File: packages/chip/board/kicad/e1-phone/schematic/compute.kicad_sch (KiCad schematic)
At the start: 0 parts

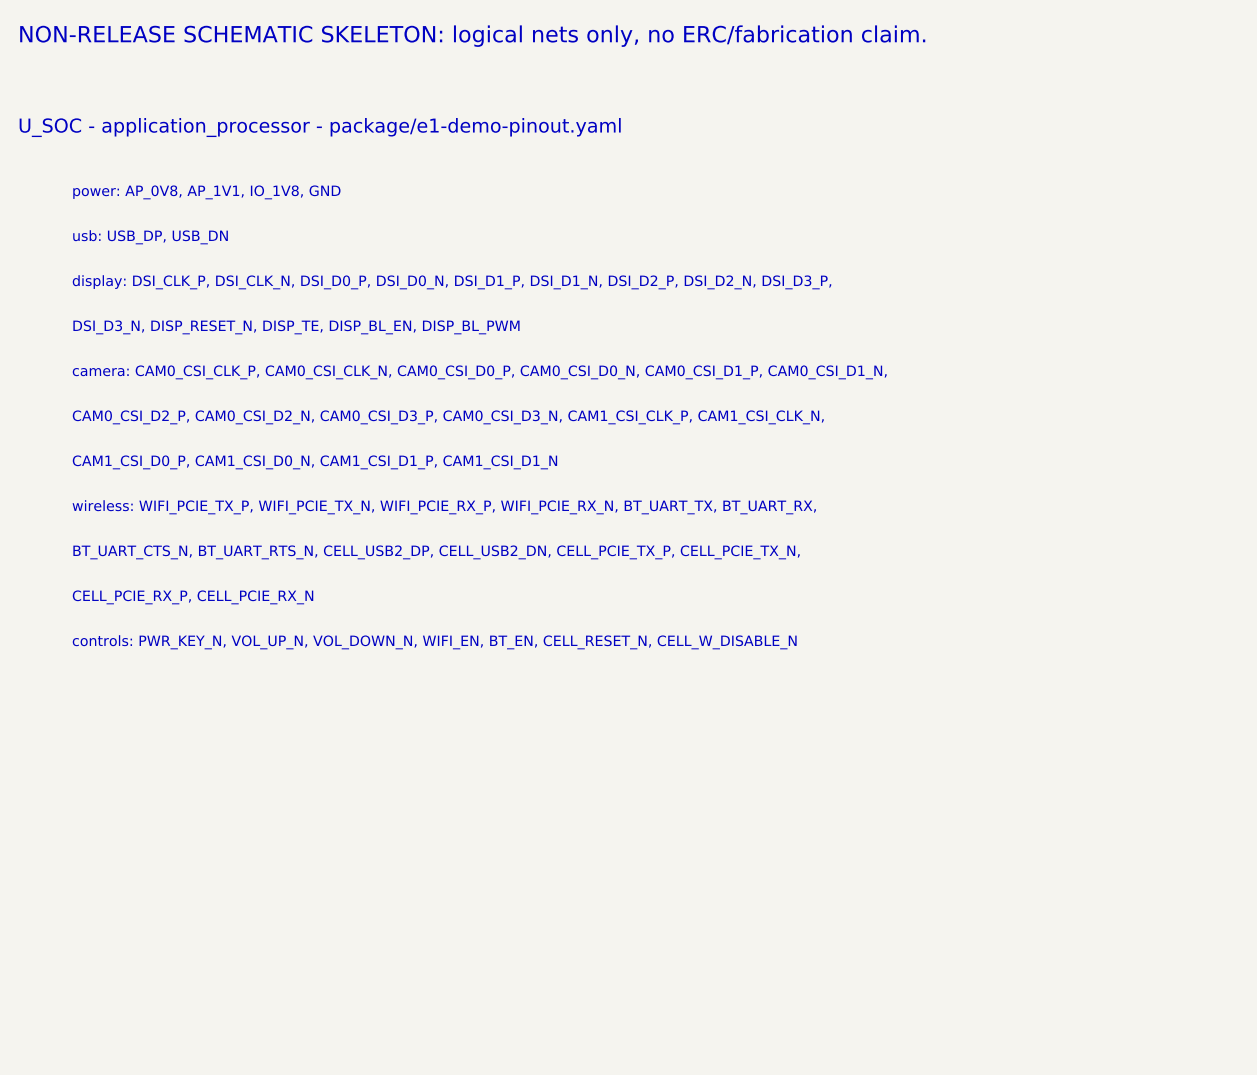
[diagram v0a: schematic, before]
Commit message: Prepare chip package for publishing
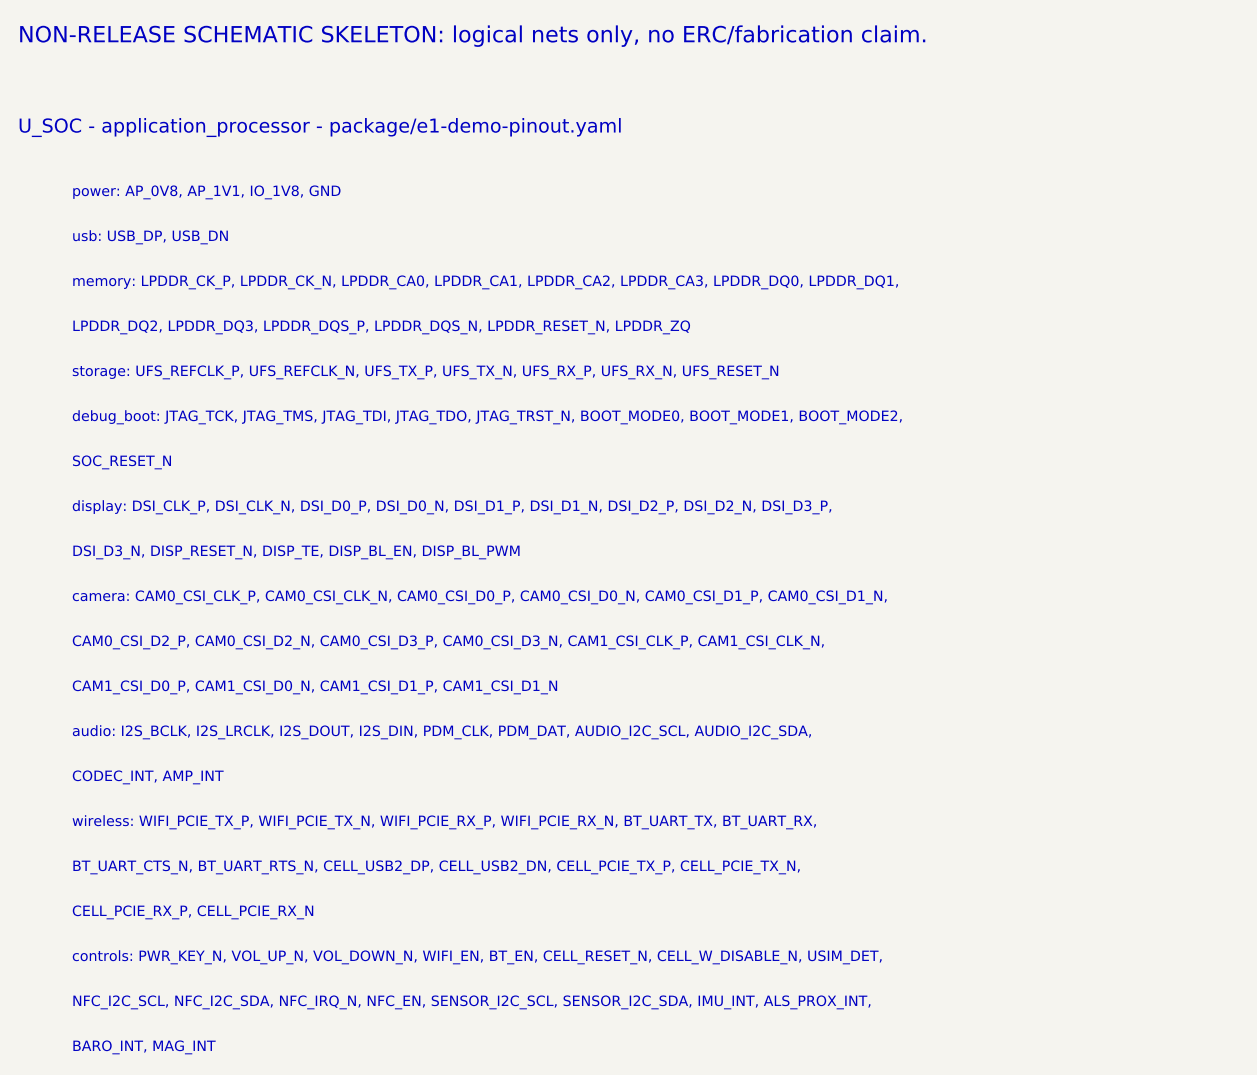
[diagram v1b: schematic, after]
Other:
- note added: "BARO_INT, MAG_INT"
- note added: "CODEC_INT, AMP_INT"
- note added: "LPDDR_DQ2, LPDDR_DQ3, LPDDR_DQS_P, LPDDR_DQS_N, LPDDR_RESET_N, LPDDR_ZQ"
- note added: "NFC_I2C_SCL, NFC_I2C_SDA, NFC_IRQ_N, NFC_EN, SENSOR_I2C_SCL, SENSOR_I2C_SDA, IMU_INT, ALS_PROX_INT,"
- note added: "SOC_RESET_N"
- note added: "audio: I2S_BCLK, I2S_LRCLK, I2S_DOUT, I2S_DIN, PDM_CLK, PDM_DAT, AUDIO_I2C_SCL, AUDIO_I2C_SDA,"
- note added: "controls: PWR_KEY_N, VOL_UP_N, VOL_DOWN_N, WIFI_EN, BT_EN, CELL_RESET_N, CELL_W_DISABLE_N, USIM_DET,"
- note added: "debug_boot: JTAG_TCK, JTAG_TMS, JTAG_TDI, JTAG_TDO, JTAG_TRST_N, BOOT_MODE0, BOOT_MODE1, BOOT_MODE2,"
- note added: "memory: LPDDR_CK_P, LPDDR_CK_N, LPDDR_CA0, LPDDR_CA1, LPDDR_CA2, LPDDR_CA3, LPDDR_DQ0, LPDDR_DQ1,"
- note added: "storage: UFS_REFCLK_P, UFS_REFCLK_N, UFS_TX_P, UFS_TX_N, UFS_RX_P, UFS_RX_N, UFS_RESET_N"
- note removed: "controls: PWR_KEY_N, VOL_UP_N, VOL_DOWN_N, WIFI_EN, BT_EN, CELL_RESET_N, CELL_W_DISABLE_N"
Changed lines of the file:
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@@
     (effects (font (size 1.15 1.15)) (justify left bottom))
   )
-  (text "display: DSI_CLK_P, DSI_CLK_N, DSI_D0_P, DSI_D0_N, DSI_D1_P, DSI_D1_N, DSI_D2_P, DSI_D2_N, DSI_D3_P," (at 26.00 47.00 0)
+  (text "memory: LPDDR_CK_P, LPDDR_CK_N, LPDDR_CA0, LPDDR_CA1, LPDDR_CA2, LPDDR_CA3, LPDDR_DQ0, LPDDR_DQ1," (at 26.00 47.00 0)
     (effects (font (size 1.15 1.15)) (justify left bottom))
   )
-  (text "DSI_D3_N, DISP_RESET_N, DISP_TE, DISP_BL_EN, DISP_BL_PWM" (at 26.00 52.00 0)
+  (text "LPDDR_DQ2, LPDDR_DQ3, LPDDR_DQS_P, LPDDR_DQS_N, LPDDR_RESET_N, LPDDR_ZQ" (at 26.00 52.00 0)
     (effects (font (size 1.15 1.15)) (justify left bottom))
   )
-  (text "camera: CAM0_CSI_CLK_P, CAM0_CSI_CLK_N, CAM0_CSI_D0_P, CAM0_CSI_D0_N, CAM0_CSI_D1_P, CAM0_CSI_D1_N," (at 26.00 57.00 0)
+  (text "storage: UFS_REFCLK_P, UFS_REFCLK_N, UFS_TX_P, UFS_TX_N, UFS_RX_P, UFS_RX_N, UFS_RESET_N" (at 26.00 57.00 0)
     (effects (font (size 1.15 1.15)) (justify left bottom))
   )
-  (text "CAM0_CSI_D2_P, CAM0_CSI_D2_N, CAM0_CSI_D3_P, CAM0_CSI_D3_N, CAM1_CSI_CLK_P, CAM1_CSI_CLK_N," (at 26.00 62.00 0)
+  (text "debug_boot: JTAG_TCK, JTAG_TMS, JTAG_TDI, JTAG_TDO, JTAG_TRST_N, BOOT_MODE0, BOOT_MODE1, BOOT_MODE2," (at 26.00 62.00 0)
     (effects (font (size 1.15 1.15)) (justify left bottom))
   )
-  (text "CAM1_CSI_D0_P, CAM1_CSI_D0_N, CAM1_CSI_D1_P, CAM1_CSI_D1_N" (at 26.00 67.00 0)
+  (text "SOC_RESET_N" (at 26.00 67.00 0)
     (effects (font (size 1.15 1.15)) (justify left bottom))
   )
-  (text "wireless: WIFI_PCIE_TX_P, WIFI_PCIE_TX_N, WIFI_PCIE_RX_P, WIFI_PCIE_RX_N, BT_UART_TX, BT_UART_RX," (at 26.00 72.00 0)
+  (text "display: DSI_CLK_P, DSI_CLK_N, DSI_D0_P, DSI_D0_N, DSI_D1_P, DSI_D1_N, DSI_D2_P, DSI_D2_N, DSI_D3_P," (at 26.00 72.00 0)
     (effects (font (size 1.15 1.15)) (justify left bottom))
   )
-  (text "BT_UART_CTS_N, BT_UART_RTS_N, CELL_USB2_DP, CELL_USB2_DN, CELL_PCIE_TX_P, CELL_PCIE_TX_N," (at 26.00 77.00 0)
+  (text "DSI_D3_N, DISP_RESET_N, DISP_TE, DISP_BL_EN, DISP_BL_PWM" (at 26.00 77.00 0)
     (effects (font (size 1.15 1.15)) (justify left bottom))
   )
-  (text "CELL_PCIE_RX_P, CELL_PCIE_RX_N" (at 26.00 82.00 0)
+  (text "camera: CAM0_CSI_CLK_P, CAM0_CSI_CLK_N, CAM0_CSI_D0_P, CAM0_CSI_D0_N, CAM0_CSI_D1_P, CAM0_CSI_D1_N," (at 26.00 82.00 0)
     (effects (font (size 1.15 1.15)) (justify left bottom))
   )
-  (text "controls: PWR_KEY_N, VOL_UP_N, VOL_DOWN_N, WIFI_EN, BT_EN, CELL_RESET_N, CELL_W_DISABLE_N" (at 26.00 87.00 0)
+  (text "CAM0_CSI_D2_P, CAM0_CSI_D2_N, CAM0_CSI_D3_P, CAM0_CSI_D3_N, CAM1_CSI_CLK_P, CAM1_CSI_CLK_N," (at 26.00 87.00 0)
     (effects (font (size 1.15 1.15)) (justify left bottom))
   )
+  (text "CAM1_CSI_D0_P, CAM1_CSI_D0_N, CAM1_CSI_D1_P, CAM1_CSI_D1_N" (at 26.00 92.00 0)
+    (effects (font (size 1.15 1.15)) (justify left bottom))
+  )
+  (text "audio: I2S_BCLK, I2S_LRCLK, I2S_DOUT, I2S_DIN, PDM_CLK, PDM_DAT, AUDIO_I2C_SCL, AUDIO_I2C_SDA," (at 26.00 97.00 0)
+    (effects (font (size 1.15 1.15)) (justify left bottom))
+  )
+  (text "CODEC_INT, AMP_INT" (at 26.00 102.00 0)
+    (effects (font (size 1.15 1.15)) (justify left bottom))
+  )
+  (text "wireless: WIFI_PCIE_TX_P, WIFI_PCIE_TX_N, WIFI_PCIE_RX_P, WIFI_PCIE_RX_N, BT_UART_TX, BT_UART_RX," (at 26.00 107.00 0)
+    (effects (font (size 1.15 1.15)) (justify left bottom))
+  )
+  (text "BT_UART_CTS_N, BT_UART_RTS_N, CELL_USB2_DP, CELL_USB2_DN, CELL_PCIE_TX_P, CELL_PCIE_TX_N," (at 26.00 112.00 0)
+    (effects (font (size 1.15 1.15)) (justify left bottom))
+  )
+  (text "CELL_PCIE_RX_P, CELL_PCIE_RX_N" (at 26.00 117.00 0)
+    (effects (font (size 1.15 1.15)) (justify left bottom))
+  )
+  (text "controls: PWR_KEY_N, VOL_UP_N, VOL_DOWN_N, WIFI_EN, BT_EN, CELL_RESET_N, CELL_W_DISABLE_N, USIM_DET," (at 26.00 122.00 0)
+    (effects (font (size 1.15 1.15)) (justify left bottom))
+  )
+  (text "NFC_I2C_SCL, NFC_I2C_SDA, NFC_IRQ_N, NFC_EN, SENSOR_I2C_SCL, SENSOR_I2C_SDA, IMU_INT, ALS_PROX_INT," (at 26.00 127.00 0)
+    (effects (font (size 1.15 1.15)) (justify left bottom))
+  )
+  (text "BARO_INT, MAG_INT" (at 26.00 132.00 0)
+    (effects (font (size 1.15 1.15)) (justify left bottom))
+  )
